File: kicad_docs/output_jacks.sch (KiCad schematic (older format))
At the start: 8 parts, among them J14 PJ301M-12, J15 PJ301M-12, J16 PJ301M-12, J17 PJ301M-12

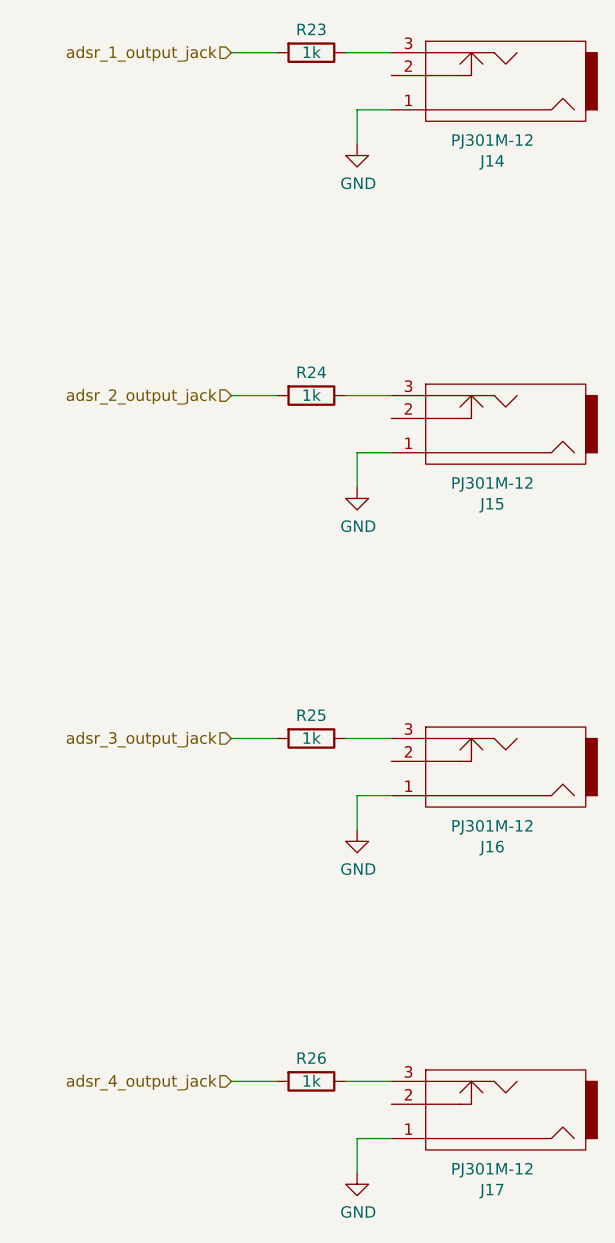
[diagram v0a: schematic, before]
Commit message: add EEPROM, big pcb re-design
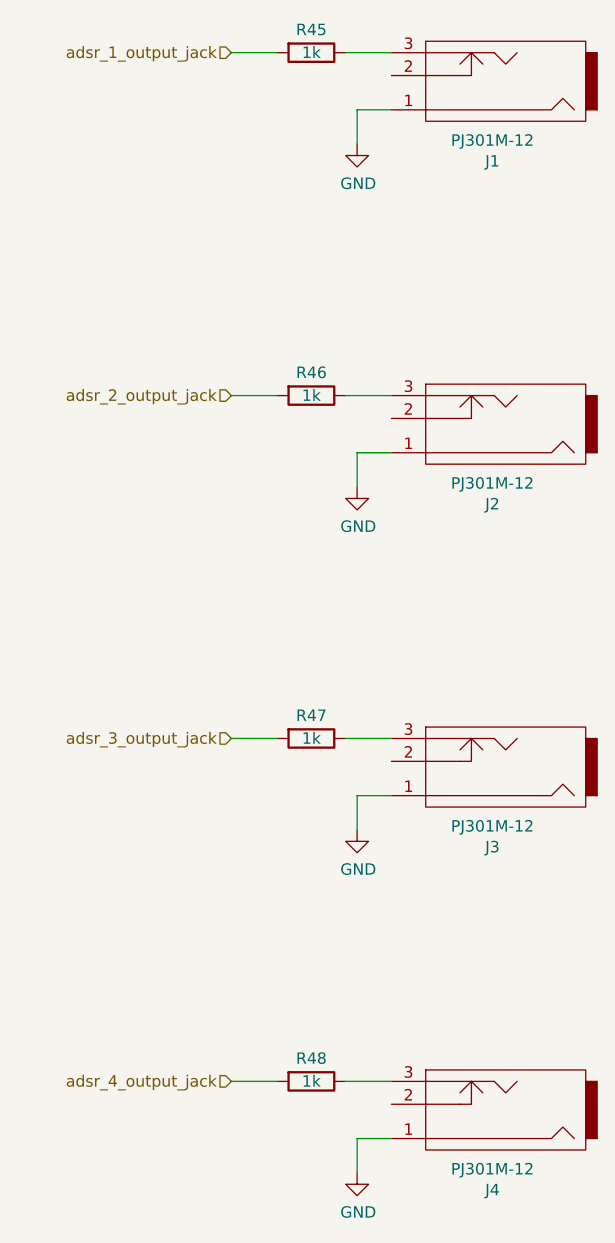
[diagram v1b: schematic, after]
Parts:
- R45: renamed from R23; footprint Resistor_SMD:R_0805_2012Metric_Pad1.15x1.40mm_HandSolder -> Resistor_SMD:R_0603_1608Metric
- R46: renamed from R24; footprint Resistor_SMD:R_0805_2012Metric_Pad1.15x1.40mm_HandSolder -> Resistor_SMD:R_0603_1608Metric
- R47: renamed from R25; footprint Resistor_SMD:R_0805_2012Metric_Pad1.15x1.40mm_HandSolder -> Resistor_SMD:R_0603_1608Metric
- R48: renamed from R26; footprint Resistor_SMD:R_0805_2012Metric_Pad1.15x1.40mm_HandSolder -> Resistor_SMD:R_0603_1608Metric
- renumbered J14 to J1, J15 to J2, J16 to J3, J17 to J4
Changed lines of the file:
@@
 $Descr A4 11693 8268
 encoding utf-8
-Sheet 5 9
+Sheet 5 10
 Title ""
 Date ""
@@
 P 5550 6100
 AR Path="/5E685C87" Ref="J?"  Part="1"
-AR Path="/5E68118F/5E685C87" Ref="J17"  Part="1"
-F 0 "J17" H 5558 6475 50  0000 C CNN
+AR Path="/5E68118F/5E685C87" Ref="J4"  Part="1"
+F 0 "J4" H 5558 6475 50  0000 C CNN
 F 1 "PJ301M-12" H 5558 6384 50  0000 C CNN
 F 2 "Eurocad:PJ301M-12" H 5550 6100 50  0001 C CNN
@@
 P 5550 4600
 AR Path="/5E685C8D" Ref="J?"  Part="1"
-AR Path="/5E68118F/5E685C8D" Ref="J16"  Part="1"
-F 0 "J16" H 5558 4975 50  0000 C CNN
+AR Path="/5E68118F/5E685C8D" Ref="J3"  Part="1"
+F 0 "J3" H 5558 4975 50  0000 C CNN
 F 1 "PJ301M-12" H 5558 4884 50  0000 C CNN
 F 2 "Eurocad:PJ301M-12" H 5550 4600 50  0001 C CNN
@@
 P 5550 3100
 AR Path="/5E685C93" Ref="J?"  Part="1"
-AR Path="/5E68118F/5E685C93" Ref="J15"  Part="1"
-F 0 "J15" H 5558 3475 50  0000 C CNN
+AR Path="/5E68118F/5E685C93" Ref="J2"  Part="1"
+F 0 "J2" H 5558 3475 50  0000 C CNN
 F 1 "PJ301M-12" H 5558 3384 50  0000 C CNN
 F 2 "Eurocad:PJ301M-12" H 5550 3100 50  0001 C CNN
@@
 P 5550 1600
 AR Path="/5E685C99" Ref="J?"  Part="1"
-AR Path="/5E68118F/5E685C99" Ref="J14"  Part="1"
-F 0 "J14" H 5558 1975 50  0000 C CNN
+AR Path="/5E68118F/5E685C99" Ref="J1"  Part="1"
+F 0 "J1" H 5558 1975 50  0000 C CNN
 F 1 "PJ301M-12" H 5558 1884 50  0000 C CNN
 F 2 "Eurocad:PJ301M-12" H 5550 1600 50  0001 C CNN
@@
 $EndComp
 $Comp
-L power:GND #PWR026
+L power:GND #PWR037
 U 1 1 5E685EE4
 P 4950 1900
-F 0 "#PWR026" H 4950 1650 50  0001 C CNN
+F 0 "#PWR037" H 4950 1650 50  0001 C CNN
 F 1 "GND" H 4955 1727 50  0000 C CNN
 F 2 "" H 4950 1900 50  0001 C CNN
@@
 	4950 1750 5100 1750
 $Comp
-L power:GND #PWR027
+L power:GND #PWR038
 U 1 1 5E686A1D
 P 4950 3400
-F 0 "#PWR027" H 4950 3150 50  0001 C CNN
+F 0 "#PWR038" H 4950 3150 50  0001 C CNN
 F 1 "GND" H 4955 3227 50  0000 C CNN
 F 2 "" H 4950 3400 50  0001 C CNN
@@
 	4950 3250 5100 3250
 $Comp
-L power:GND #PWR028
+L power:GND #PWR039
 U 1 1 5E686FAB
 P 4950 4900
-F 0 "#PWR028" H 4950 4650 50  0001 C CNN
+F 0 "#PWR039" H 4950 4650 50  0001 C CNN
 F 1 "GND" H 4955 4727 50  0000 C CNN
 F 2 "" H 4950 4900 50  0001 C CNN
@@
 	4950 4750 5100 4750
 $Comp
-L power:GND #PWR029
+L power:GND #PWR040
 U 1 1 5E6872DD
 P 4950 6400
-F 0 "#PWR029" H 4950 6150 50  0001 C CNN
+F 0 "#PWR040" H 4950 6150 50  0001 C CNN
 F 1 "GND" H 4955 6227 50  0000 C CNN
 F 2 "" H 4950 6400 50  0001 C CNN
@@
 	4950 6250 5100 6250
 $Comp
-L Device:R R23
+L Device:R R45
 U 1 1 5E68763A
 P 4750 1500
-F 0 "R23" V 4650 1500 50  0000 C CNN
+F 0 "R45" V 4650 1500 50  0000 C CNN
 F 1 "1k" V 4750 1500 50  0000 C CNN
-F 2 "Resistor_SMD:R_0805_2012Metric_Pad1.15x1.40mm_HandSolder" V 4680 1500 50  0001 C CNN
+F 2 "Resistor_SMD:R_0603_1608Metric" V 4680 1500 50  0001 C CNN
 F 3 "~" H 4750 1500 50  0001 C CNN
 	1    4750 1500
@@
 	4400 1500 4600 1500
 $Comp
-L Device:R R24
+L Device:R R46
 U 1 1 5E689304
 P 4750 3000
-F 0 "R24" V 4650 3000 50  0000 C CNN
+F 0 "R46" V 4650 3000 50  0000 C CNN
 F 1 "1k" V 4750 3000 50  0000 C CNN
-F 2 "Resistor_SMD:R_0805_2012Metric_Pad1.15x1.40mm_HandSolder" V 4680 3000 50  0001 C CNN
+F 2 "Resistor_SMD:R_0603_1608Metric" V 4680 3000 50  0001 C CNN
 F 3 "~" H 4750 3000 50  0001 C CNN
 	1    4750 3000
@@
 	4400 3000 4600 3000
 $Comp
-L Device:R R25
+L Device:R R47
 U 1 1 5E6898B6
 P 4750 4500
-F 0 "R25" V 4650 4500 50  0000 C CNN
+F 0 "R47" V 4650 4500 50  0000 C CNN
 F 1 "1k" V 4750 4500 50  0000 C CNN
-F 2 "Resistor_SMD:R_0805_2012Metric_Pad1.15x1.40mm_HandSolder" V 4680 4500 50  0001 C CNN
+F 2 "Resistor_SMD:R_0603_1608Metric" V 4680 4500 50  0001 C CNN
 F 3 "~" H 4750 4500 50  0001 C CNN
 	1    4750 4500
@@
 	4400 4500 4600 4500
 $Comp
-L Device:R R26
+L Device:R R48
 U 1 1 5E689D56
 P 4750 6000
-F 0 "R26" V 4650 6000 50  0000 C CNN
+F 0 "R48" V 4650 6000 50  0000 C CNN
 F 1 "1k" V 4750 6000 50  0000 C CNN
-F 2 "Resistor_SMD:R_0805_2012Metric_Pad1.15x1.40mm_HandSolder" V 4680 6000 50  0001 C CNN
+F 2 "Resistor_SMD:R_0603_1608Metric" V 4680 6000 50  0001 C CNN
 F 3 "~" H 4750 6000 50  0001 C CNN
 	1    4750 6000
